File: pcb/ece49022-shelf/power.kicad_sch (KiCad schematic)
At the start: 13 parts, among them U1 TPS54202DDCT

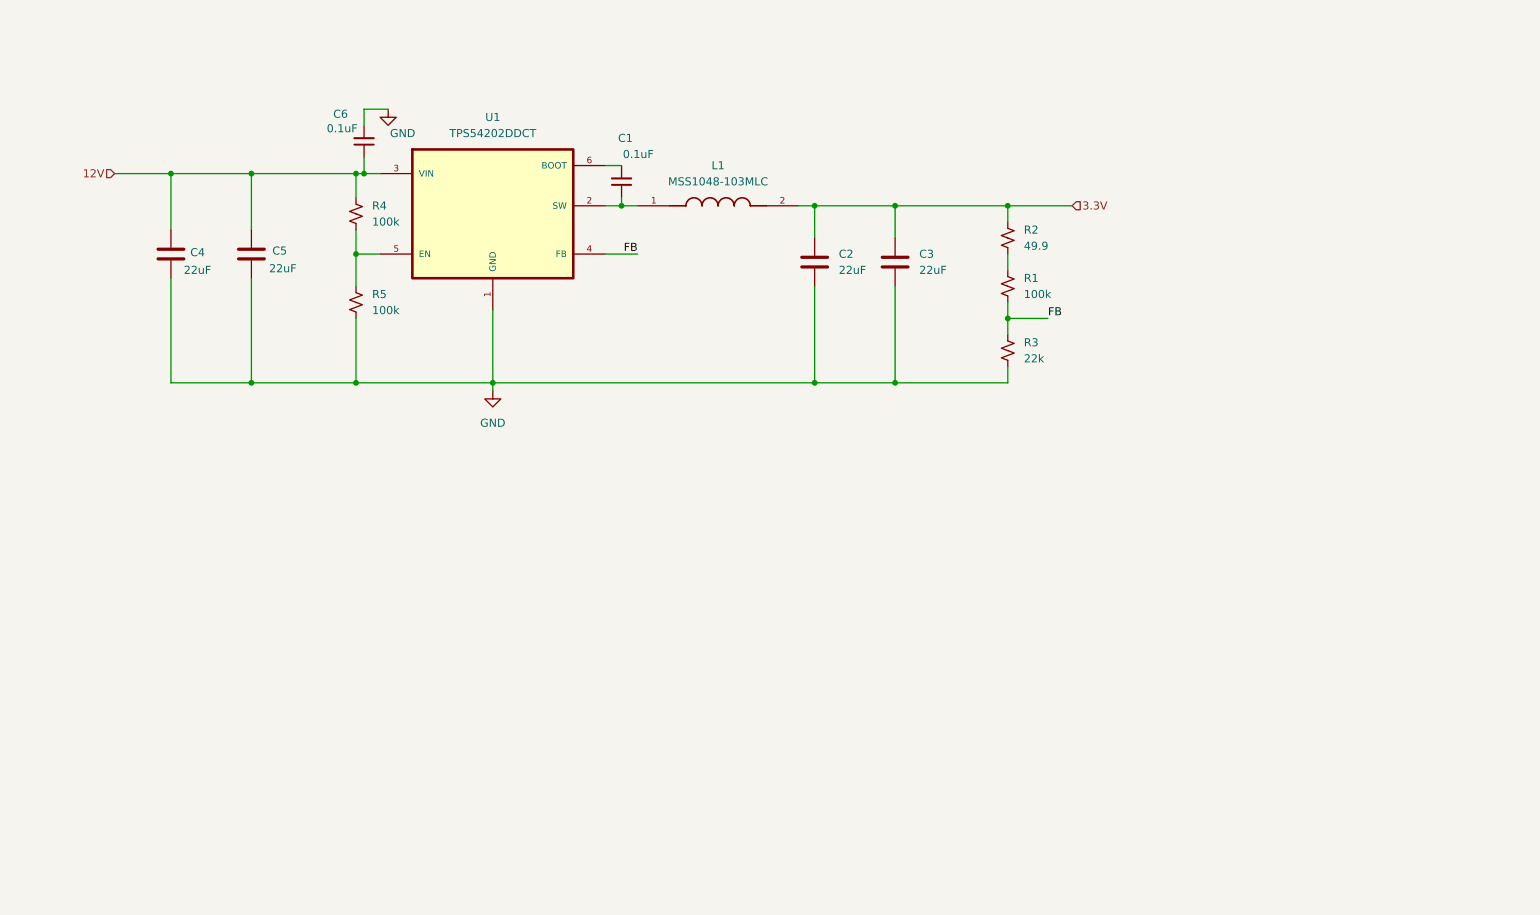
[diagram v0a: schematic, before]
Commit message: Initial Power Schematics Finished
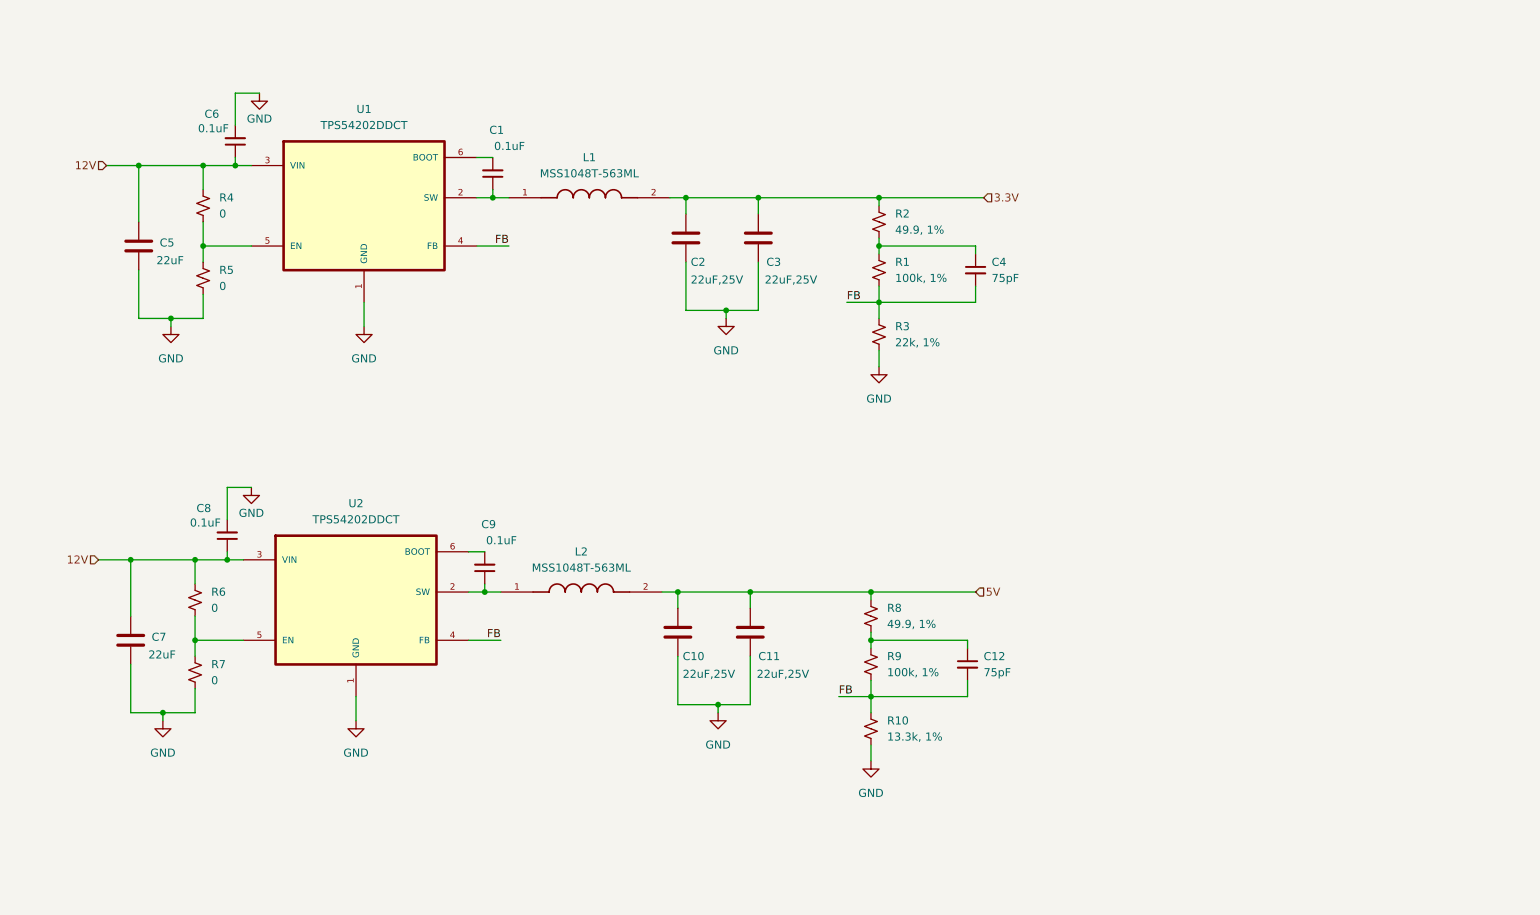
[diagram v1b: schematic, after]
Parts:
- removed C4: 22uF, Capacitor_SMD:C_0805_2012Metric_Pad1.18x1.45mm_HandSolder, symbol Device:C
- added C10, C11: 22uF,25V, Capacitor_SMD:C_0805_2012Metric_Pad1.18x1.45mm_HandSolder, symbol Device:C
- added C12, C4: 75pF, Capacitor_SMD:C_0402_1005Metric, symbol Device:C_Small
- added C7: 22uF, Capacitor_SMD:C_0805_2012Metric_Pad1.18x1.45mm_HandSolder, symbol Device:C
- added C8, C9: 0.1uF, Capacitor_SMD:C_0402_1005Metric, symbol Device:C_Small
- added L2: MSS1048T-563ML, 49022_Footprints:IND_MSS1048, symbol ECE49022_Symbols:MSS1048-103MLC
- added R10: 13.3k, 1%, Capacitor_SMD:C_0402_1005Metric, symbol Device:R_Small_US
- added R6, R7: 0, Capacitor_SMD:C_0402_1005Metric, symbol Device:R_Small_US
- added R8: 49.9, 1%, Capacitor_SMD:C_0402_1005Metric, symbol Device:R_Small_US
- added R9: 100k, 1%, Capacitor_SMD:C_0402_1005Metric, symbol Device:R_Small_US
- added U2: TPS54202DDCT, 49022_Footprints:TPS54202, symbol ECE49022_Symbols:TPS54202DDCT
- C2, C3: value 22uF -> 22uF,25V
- L1: value MSS1048-103MLC -> MSS1048T-563ML
- R1: value 100k -> 100k, 1%; footprint (none) -> Capacitor_SMD:C_0402_1005Metric
- R2: value 49.9 -> 49.9, 1%; footprint (none) -> Capacitor_SMD:C_0402_1005Metric
- R3: value 22k -> 22k, 1%; footprint (none) -> Capacitor_SMD:C_0402_1005Metric
- R4, R5: value 100k -> 0; footprint (none) -> Capacitor_SMD:C_0402_1005Metric
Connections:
- net 12V: now also C7.1, C8.1, R6.1, U2.3 (VIN)
- net FB: now also C12.2, C4.2, R10.1, R9.2, U2.4 (FB)
- net GND: now also C10.2, C11.2, C7.2, C8.2, R10.2, R7.2, U2.1 (GND)
- net at R1.1, R2.2: now also C4.1
- new net: C9.1, L2.1, U2.2 (SW)
- new net: C9.2, U2.6 (BOOT)
- new net: C12.1, R8.2, R9.1
- new net: R6.2, R7.1, U2.5 (EN)
- new net 5V: C10.1, C11.1, L2.2, R8.1
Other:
- moved on the sheet: C1, C2, C3, C5, C6, L1, R1, R2, R3, R4, U1

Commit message: connecting top level
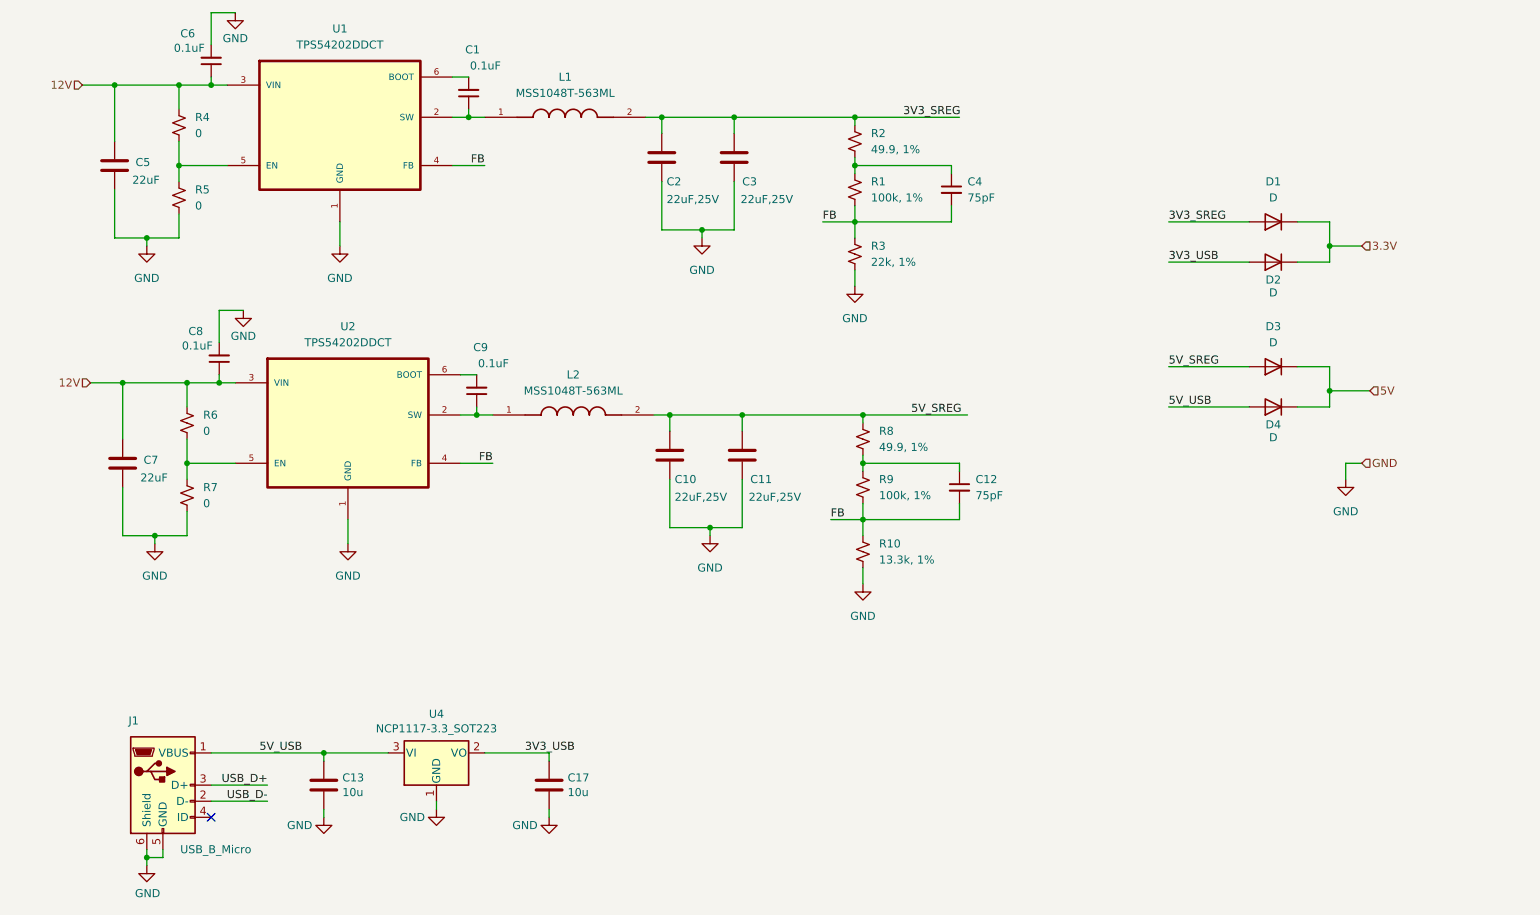
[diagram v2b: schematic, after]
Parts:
- added C13, C17: 10u, Capacitor_SMD:C_0805_2012Metric, symbol Device:C
- added D1, D2, D3, D4: D, symbol Device:D
- added J1: USB_B_Micro, 49022_Footprints:USB_Micro-B_Amphenol_10103594-0001LF_Horizontal_modified, symbol Connector:USB_B_Micro
- added U4: NCP1117-3.3_SOT223, Package_TO_SOT_SMD:SOT-223-3_TabPin2, symbol Regulator_Linear:NCP1117-3.3_SOT223
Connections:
- net 3.3V: now also D1.1 (K), D2.1 (K); no longer C2.1, C3.1, L1.2, R2.1
- net 5V: now also D3.1 (K), D4.1 (K); no longer C10.1, C11.1, L2.2, R8.1
- net GND: now also C13.2, C17.2, J1.5 (GND), J1.6 (Shield), U4.1 (GND)
- new net 3V3_SREG: C2.1, C3.1, D1.2 (A), L1.2, R2.1
- new net 3V3_USB: C17.1, D2.2 (A), U4.2 (VO)
- new net 5V_SREG: C10.1, C11.1, D3.2 (A), L2.2, R8.1
- new net 5V_USB: C13.1, D4.2 (A), J1.1 (VBUS), U4.3 (VI)
- new net USB_D+: J1.3 (D+)
- new net USB_D-: J1.2 (D-)
- no-connect marks 0 -> 1
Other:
- moved on the sheet: C1, C10, C11, C12, C2, C3, C4, C5, C6, C7, C8, C9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

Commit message: edited shelf power and added power for interface PCB
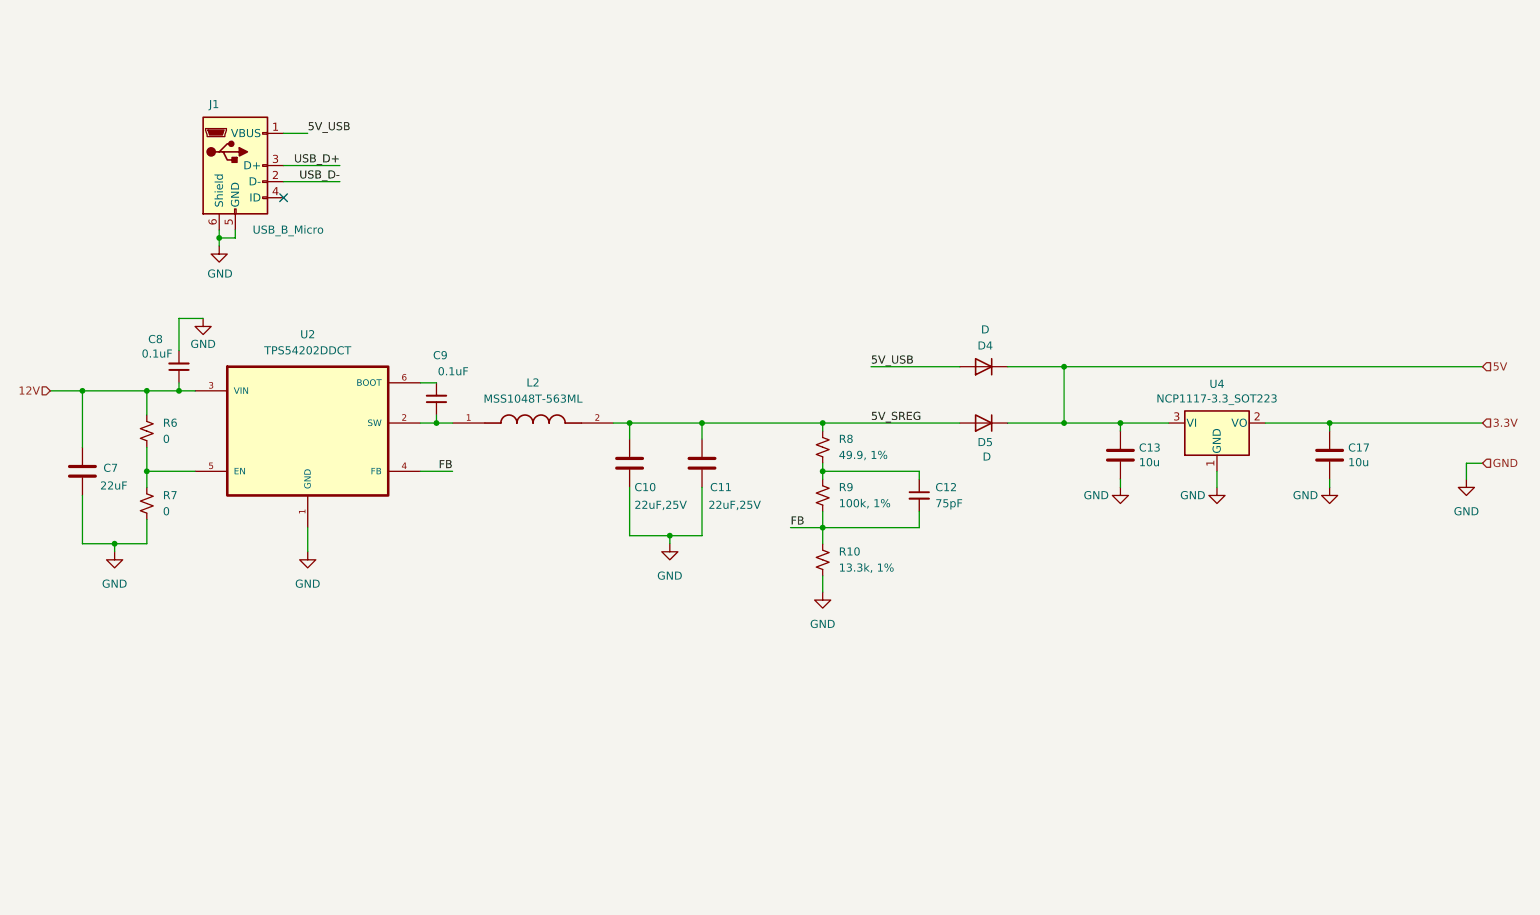
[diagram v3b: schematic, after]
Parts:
- removed C1, C6: 0.1uF, Capacitor_SMD:C_0402_1005Metric, symbol Device:C_Small
- removed C2, C3: 22uF,25V, Capacitor_SMD:C_0805_2012Metric_Pad1.18x1.45mm_HandSolder, symbol Device:C
- removed C4: 75pF, Capacitor_SMD:C_0402_1005Metric, symbol Device:C_Small
- removed C5: 22uF, Capacitor_SMD:C_0805_2012Metric_Pad1.18x1.45mm_HandSolder, symbol Device:C
- removed D1, D2, D3: D, symbol Device:D
- removed L1: MSS1048T-563ML, 49022_Footprints:IND_MSS1048, symbol ECE49022_Symbols:MSS1048-103MLC
- removed R1: 100k, 1%, Capacitor_SMD:C_0402_1005Metric, symbol Device:R_Small_US
- removed R2: 49.9, 1%, Capacitor_SMD:C_0402_1005Metric, symbol Device:R_Small_US
- removed R3: 22k, 1%, Capacitor_SMD:C_0402_1005Metric, symbol Device:R_Small_US
- removed R4, R5: 0, Capacitor_SMD:C_0402_1005Metric, symbol Device:R_Small_US
- removed U1: TPS54202DDCT, 49022_Footprints:TPS54202, symbol ECE49022_Symbols:TPS54202DDCT
- added D5: D, symbol Device:D
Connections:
- net 3V3_USB is gone; now on net 3.3V: C17.1, U4.2 (VO)
- net 5V: now also C13.1, U4.3 (VI), D5.1 (K)
- net 5V_SREG: now also D5.2 (A)
- net 5V_USB: no longer C13.1, U4.3 (VI)
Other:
- moved on the sheet: C10, C11, C12, C13, C17, C7, C8, C9, D4, J1, L2, R10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

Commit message: Added components and got pcb layout imported
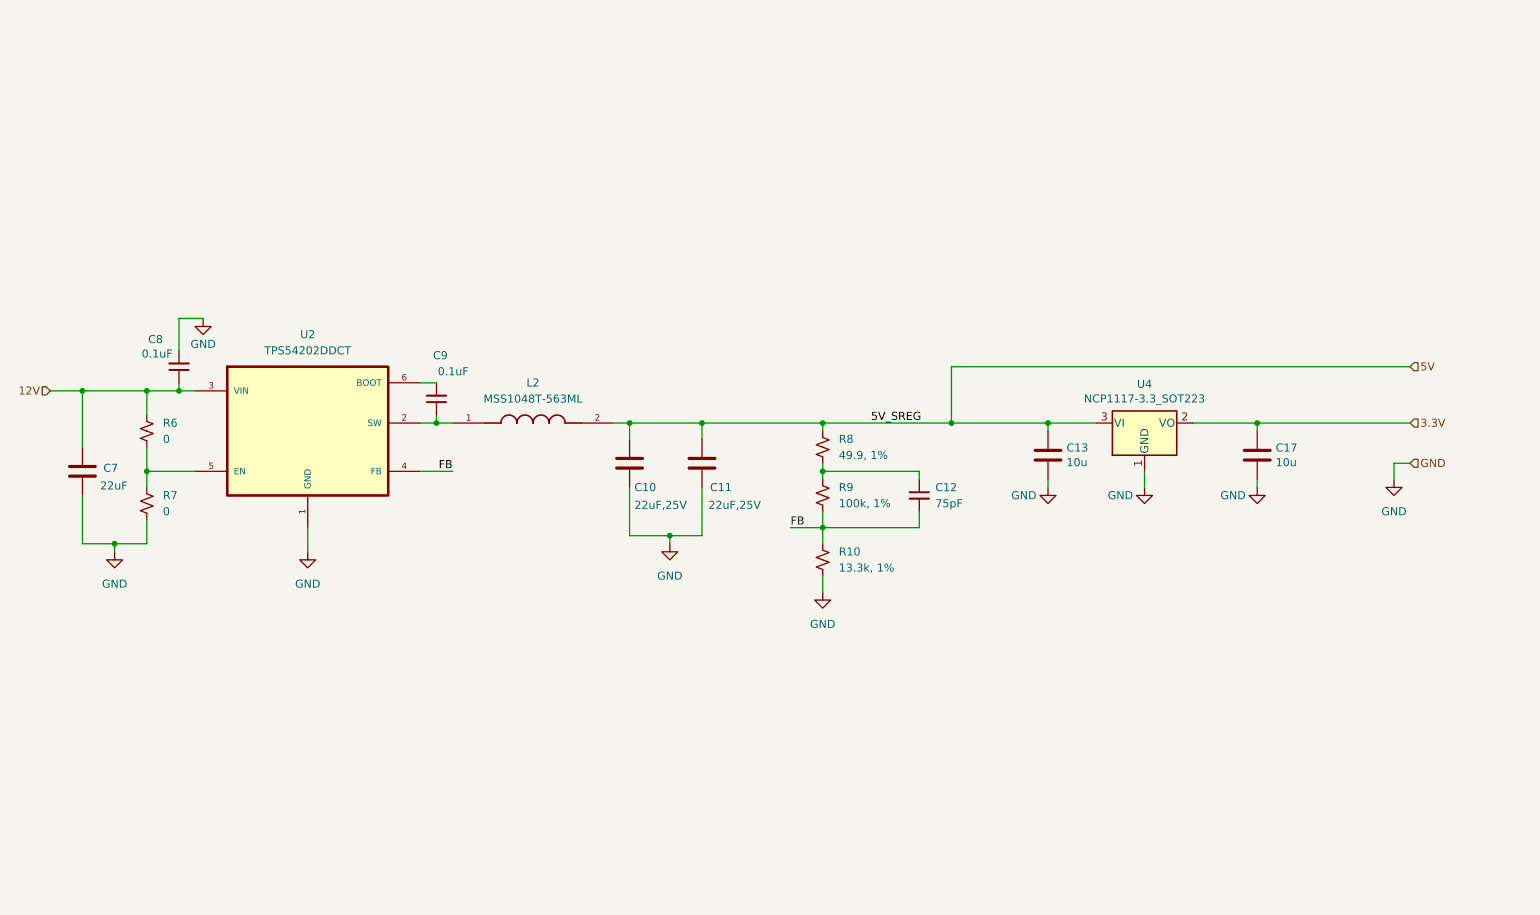
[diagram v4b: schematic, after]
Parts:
- removed D4, D5: D, symbol Device:D
- removed J1: USB_B_Micro, 49022_Footprints:USB_Micro-B_Amphenol_10103594-0001LF_Horizontal_modified, symbol Connector:USB_B_Micro
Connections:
- net 5V_SREG is gone; now on net 5V: C10.1, C11.1, L2.2, R8.1
- no-connect marks 1 -> 0
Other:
- moved on the sheet: C13, C17, U4

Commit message: stuff
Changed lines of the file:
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@@
 	)
 	(label "5V_SREG"
-		(at 152.4 87.63 0)
+		(at 149.86 87.63 0)
 		(effects
 			(font

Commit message: stuff
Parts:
- R6: value 0 -> 510K
- R7: value 0 -> 105k
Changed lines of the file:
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@@
 			)
 		)
-		(property "Value" "0"
+		(property "Value" "105k"
 			(at 40.64 101.5999 0)
 			(effects
@@
 			)
 		)
-		(property "Value" "0"
+		(property "Value" "510K"
 			(at 40.64 90.1699 0)
 			(effects
